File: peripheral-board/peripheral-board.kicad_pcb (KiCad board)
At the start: 2 copper layers, 165 x 100 mm, 0 parts

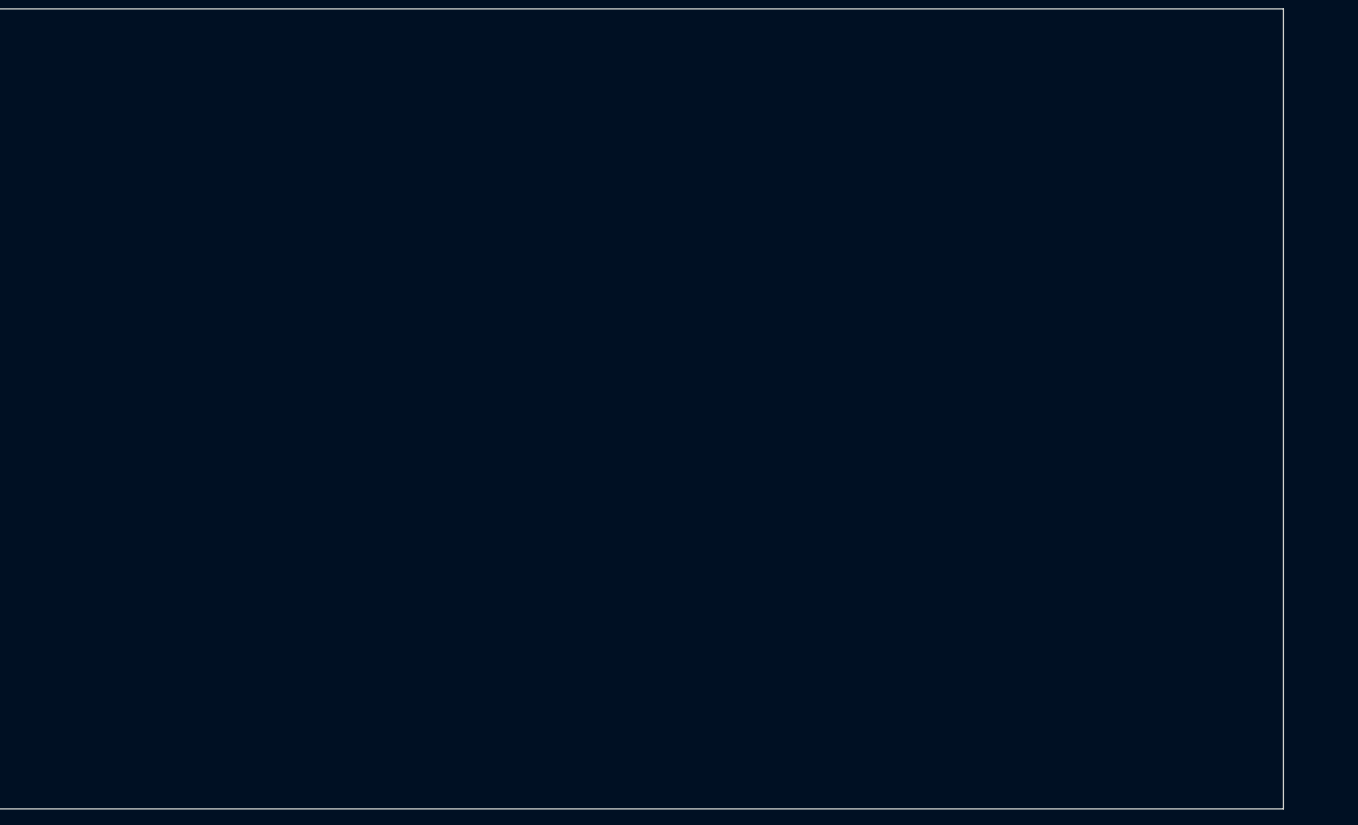
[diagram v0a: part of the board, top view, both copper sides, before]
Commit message: added button 3d model
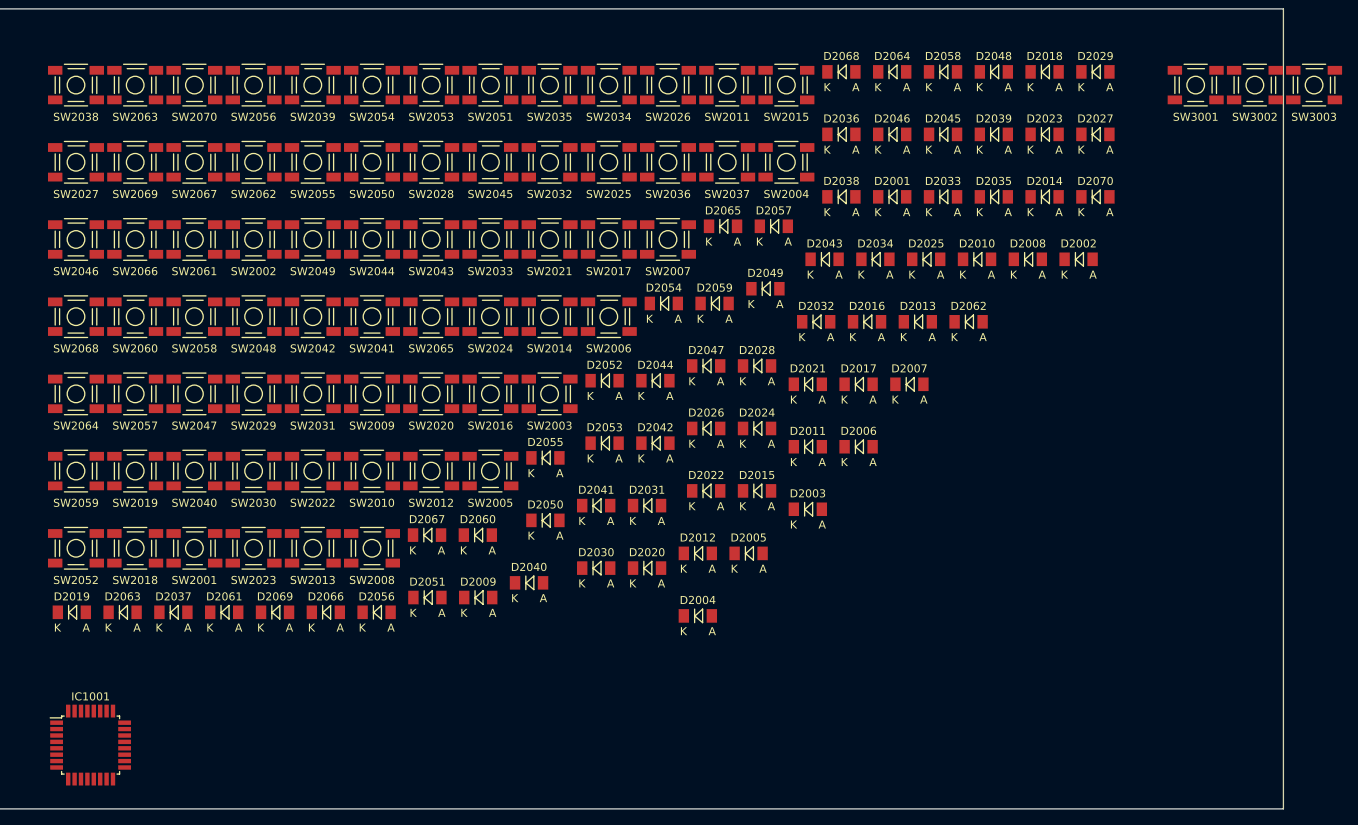
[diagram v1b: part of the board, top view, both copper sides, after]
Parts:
- added D2001: 1N4148, Diodes_SMD:MiniMELF_Standard, F.Cu at (176.1, 68.5)
- added D2002: 1N4148, Diodes_SMD:MiniMELF_Standard, F.Cu at (199.4, 76.3)
- added D2003: 1N4148, Diodes_SMD:MiniMELF_Standard, F.Cu at (165.6, 107.5)
- added D2004: 1N4148, Diodes_SMD:MiniMELF_Standard, F.Cu at (151.8, 120.9)
- added D2005: 1N4148, Diodes_SMD:MiniMELF_Standard, F.Cu at (158.2, 113.1)
- added D2006: 1N4148, Diodes_SMD:MiniMELF_Standard, F.Cu at (171.9, 99.7)
- added D2007: 1N4148, Diodes_SMD:MiniMELF_Standard, F.Cu at (178.3, 91.9)
- added D2008: 1N4148, Diodes_SMD:MiniMELF_Standard, F.Cu at (193.1, 76.3)
- added D2009: 1N4148, Diodes_SMD:MiniMELF_Standard, F.Cu at (124.4, 118.6)
- added D2010: 1N4148, Diodes_SMD:MiniMELF_Standard, F.Cu at (186.7, 76.3)
- added D2011: 1N4148, Diodes_SMD:MiniMELF_Standard, F.Cu at (165.6, 99.7)
- added D2012: 1N4148, Diodes_SMD:MiniMELF_Standard, F.Cu at (151.8, 113.1)
- added D2013: 1N4148, Diodes_SMD:MiniMELF_Standard, F.Cu at (179.3, 84.1)
- added D2014: 1N4148, Diodes_SMD:MiniMELF_Standard, F.Cu at (195.2, 68.5)
- added D2015: 1N4148, Diodes_SMD:MiniMELF_Standard, F.Cu at (159.2, 105.3)
- added D2016: 1N4148, Diodes_SMD:MiniMELF_Standard, F.Cu at (173.0, 84.1)
- added D2017: 1N4148, Diodes_SMD:MiniMELF_Standard, F.Cu at (171.9, 91.9)
- added D2018: 1N4148, Diodes_SMD:MiniMELF_Standard, F.Cu at (195.2, 52.9)
- added D2019: 1N4148, Diodes_SMD:MiniMELF_Standard, F.Cu at (73.6, 120.4)
- added D2020: 1N4148, Diodes_SMD:MiniMELF_Standard, F.Cu at (145.5, 114.9)
- added D2021: 1N4148, Diodes_SMD:MiniMELF_Standard, F.Cu at (165.6, 91.9)
- added D2022: 1N4148, Diodes_SMD:MiniMELF_Standard, F.Cu at (152.9, 105.3)
- added D2023: 1N4148, Diodes_SMD:MiniMELF_Standard, F.Cu at (195.2, 60.7)
- added D2024: 1N4148, Diodes_SMD:MiniMELF_Standard, F.Cu at (159.2, 97.4)
- added D2025: 1N4148, Diodes_SMD:MiniMELF_Standard, F.Cu at (180.4, 76.3)
- added D2026: 1N4148, Diodes_SMD:MiniMELF_Standard, F.Cu at (152.9, 97.4)
- added D2027: 1N4148, Diodes_SMD:MiniMELF_Standard, F.Cu at (201.5, 60.7)
- added D2028: 1N4148, Diodes_SMD:MiniMELF_Standard, F.Cu at (159.2, 89.6)
- added D2029: 1N4148, Diodes_SMD:MiniMELF_Standard, F.Cu at (201.5, 52.9)
- added D2030: 1N4148, Diodes_SMD:MiniMELF_Standard, F.Cu at (139.1, 114.9)
- added D2031: 1N4148, Diodes_SMD:MiniMELF_Standard, F.Cu at (145.5, 107.1)
- added D2032: 1N4148, Diodes_SMD:MiniMELF_Standard, F.Cu at (166.6, 84.1)
- added D2033: 1N4148, Diodes_SMD:MiniMELF_Standard, F.Cu at (182.5, 68.5)
- added D2034: 1N4148, Diodes_SMD:MiniMELF_Standard, F.Cu at (174.0, 76.3)
- added D2035: 1N4148, Diodes_SMD:MiniMELF_Standard, F.Cu at (188.8, 68.5)
- added D2036: 1N4148, Diodes_SMD:MiniMELF_Standard, F.Cu at (169.8, 60.7)
- added D2037: 1N4148, Diodes_SMD:MiniMELF_Standard, F.Cu at (86.3, 120.4)
- added D2038: 1N4148, Diodes_SMD:MiniMELF_Standard, F.Cu at (169.8, 68.5)
- added D2039: 1N4148, Diodes_SMD:MiniMELF_Standard, F.Cu at (188.8, 60.7)
- added D2040: 1N4148, Diodes_SMD:MiniMELF_Standard, F.Cu at (130.7, 116.7)
- added D2041: 1N4148, Diodes_SMD:MiniMELF_Standard, F.Cu at (139.1, 107.1)
- added D2042: 1N4148, Diodes_SMD:MiniMELF_Standard, F.Cu at (146.5, 99.3)
- added D2043: 1N4148, Diodes_SMD:MiniMELF_Standard, F.Cu at (167.7, 76.3)
- added D2044: 1N4148, Diodes_SMD:MiniMELF_Standard, F.Cu at (146.5, 91.5)
- added D2045: 1N4148, Diodes_SMD:MiniMELF_Standard, F.Cu at (182.5, 60.7)
- added D2046: 1N4148, Diodes_SMD:MiniMELF_Standard, F.Cu at (176.1, 60.7)
- added D2047: 1N4148, Diodes_SMD:MiniMELF_Standard, F.Cu at (152.9, 89.6)
- added D2048: 1N4148, Diodes_SMD:MiniMELF_Standard, F.Cu at (188.8, 52.9)
- added D2049: 1N4148, Diodes_SMD:MiniMELF_Standard, F.Cu at (160.3, 80.0)
- added D2050: 1N4148, Diodes_SMD:MiniMELF_Standard, F.Cu at (132.8, 108.9)
- added D2051: 1N4148, Diodes_SMD:MiniMELF_Standard, F.Cu at (118.0, 118.6)
- added D2052: 1N4148, Diodes_SMD:MiniMELF_Standard, F.Cu at (140.2, 91.5)
- added D2053: 1N4148, Diodes_SMD:MiniMELF_Standard, F.Cu at (140.2, 99.3)
- added D2054: 1N4148, Diodes_SMD:MiniMELF_Standard, F.Cu at (147.6, 81.8)
- added D2055: 1N4148, Diodes_SMD:MiniMELF_Standard, F.Cu at (132.8, 101.1)
- added D2056: 1N4148, Diodes_SMD:MiniMELF_Standard, F.Cu at (111.7, 120.4)
- added D2057: 1N4148, Diodes_SMD:MiniMELF_Standard, F.Cu at (161.3, 72.2)
- added D2058: 1N4148, Diodes_SMD:MiniMELF_Standard, F.Cu at (182.5, 52.9)
- added D2059: 1N4148, Diodes_SMD:MiniMELF_Standard, F.Cu at (153.9, 81.8)
- added D2060: 1N4148, Diodes_SMD:MiniMELF_Standard, F.Cu at (124.3, 110.8)
- added D2061: 1N4148, Diodes_SMD:MiniMELF_Standard, F.Cu at (92.6, 120.4)
- added D2062: 1N4148, Diodes_SMD:MiniMELF_Standard, F.Cu at (185.7, 84.1)
- added D2063: 1N4148, Diodes_SMD:MiniMELF_Standard, F.Cu at (79.9, 120.4)
- added D2064: 1N4148, Diodes_SMD:MiniMELF_Standard, F.Cu at (176.1, 52.9)
- added D2065: 1N4148, Diodes_SMD:MiniMELF_Standard, F.Cu at (155.0, 72.2)
- added D2066: 1N4148, Diodes_SMD:MiniMELF_Standard, F.Cu at (105.3, 120.4)
- added D2067: 1N4148, Diodes_SMD:MiniMELF_Standard, F.Cu at (118.0, 110.8)
- added D2068: 1N4148, Diodes_SMD:MiniMELF_Standard, F.Cu at (169.8, 52.9)
- added D2069: 1N4148, Diodes_SMD:MiniMELF_Standard, F.Cu at (99.0, 120.4)
- added D2070: 1N4148, Diodes_SMD:MiniMELF_Standard, F.Cu at (201.5, 68.5)
- added IC1001: ATTINY48-A, Housings_QFP:TQFP-32_7x7mm_Pitch0.8mm, F.Cu at (75.9, 137.0)
- added SW2001: 1, lib:SMD-TACT-5.2x5.2x2mm, F.Cu at (88.9, 112.4)
- added SW2002: 2, lib:SMD-TACT-5.2x5.2x2mm, F.Cu at (96.3, 73.8)
- added SW2003: 3, lib:SMD-TACT-5.2x5.2x2mm, F.Cu at (133.3, 93.1)
- added SW2004: 4, lib:SMD-TACT-5.2x5.2x2mm, F.Cu at (162.9, 64.2)
- added SW2005: 5, lib:SMD-TACT-5.2x5.2x2mm, F.Cu at (125.9, 102.8)
- added SW2006: 6, lib:SMD-TACT-5.2x5.2x2mm, F.Cu at (140.7, 83.5)
- added SW2007: 7, lib:SMD-TACT-5.2x5.2x2mm, F.Cu at (148.1, 73.8)
- added SW2008: 8, lib:SMD-TACT-5.2x5.2x2mm, F.Cu at (111.1, 112.4)
- added SW2009: 9, lib:SMD-TACT-5.2x5.2x2mm, F.Cu at (111.1, 93.1)
- added SW2010: 0, lib:SMD-TACT-5.2x5.2x2mm, F.Cu at (111.1, 102.8)
- added SW2011: 1, lib:SMD-TACT-5.2x5.2x2mm, F.Cu at (155.5, 54.5)
- added SW2012: 2, lib:SMD-TACT-5.2x5.2x2mm, F.Cu at (118.5, 102.8)
- added SW2013: 3, lib:SMD-TACT-5.2x5.2x2mm, F.Cu at (103.7, 112.4)
- added SW2014: 4, lib:SMD-TACT-5.2x5.2x2mm, F.Cu at (133.3, 83.5)
- added SW2015: 5, lib:SMD-TACT-5.2x5.2x2mm, F.Cu at (162.9, 54.5)
- added SW2016: 6, lib:SMD-TACT-5.2x5.2x2mm, F.Cu at (125.9, 93.1)
- added SW2017: 7, lib:SMD-TACT-5.2x5.2x2mm, F.Cu at (140.7, 73.8)
- added SW2018: 8, lib:SMD-TACT-5.2x5.2x2mm, F.Cu at (81.5, 112.4)
- added SW2019: 9, lib:SMD-TACT-5.2x5.2x2mm, F.Cu at (81.5, 102.8)
- added SW2020: 0, lib:SMD-TACT-5.2x5.2x2mm, F.Cu at (118.5, 93.1)
- added SW2021: Q, lib:SMD-TACT-5.2x5.2x2mm, F.Cu at (133.3, 73.8)
- added SW2022: W, lib:SMD-TACT-5.2x5.2x2mm, F.Cu at (103.7, 102.8)
- added SW2023: E, lib:SMD-TACT-5.2x5.2x2mm, F.Cu at (96.3, 112.4)
- added SW2024: R, lib:SMD-TACT-5.2x5.2x2mm, F.Cu at (125.9, 83.5)
- added SW2025: T, lib:SMD-TACT-5.2x5.2x2mm, F.Cu at (140.7, 64.2)
- added SW2026: Y, lib:SMD-TACT-5.2x5.2x2mm, F.Cu at (148.1, 54.5)
- added SW2027: U, lib:SMD-TACT-5.2x5.2x2mm, F.Cu at (74.1, 64.2)
- added SW2028: I, lib:SMD-TACT-5.2x5.2x2mm, F.Cu at (118.5, 64.2)
- added SW2029: O, lib:SMD-TACT-5.2x5.2x2mm, F.Cu at (96.3, 93.1)
- added SW2030: P, lib:SMD-TACT-5.2x5.2x2mm, F.Cu at (96.3, 102.8)
- added SW2031: Q, lib:SMD-TACT-5.2x5.2x2mm, F.Cu at (103.7, 93.1)
- added SW2032: W, lib:SMD-TACT-5.2x5.2x2mm, F.Cu at (133.3, 64.2)
- added SW2033: E, lib:SMD-TACT-5.2x5.2x2mm, F.Cu at (125.9, 73.8)
- added SW2034: R, lib:SMD-TACT-5.2x5.2x2mm, F.Cu at (140.7, 54.5)
- added SW2035: T, lib:SMD-TACT-5.2x5.2x2mm, F.Cu at (133.3, 54.5)
- added SW2036: Y, lib:SMD-TACT-5.2x5.2x2mm, F.Cu at (148.1, 64.2)
- added SW2037: U, lib:SMD-TACT-5.2x5.2x2mm, F.Cu at (155.5, 64.2)
- added SW2038: I, lib:SMD-TACT-5.2x5.2x2mm, F.Cu at (74.1, 54.5)
- added SW2039: O, lib:SMD-TACT-5.2x5.2x2mm, F.Cu at (103.7, 54.5)
- added SW2040: P, lib:SMD-TACT-5.2x5.2x2mm, F.Cu at (88.9, 102.8)
- added SW2041: A, lib:SMD-TACT-5.2x5.2x2mm, F.Cu at (111.1, 83.5)
- added SW2042: S, lib:SMD-TACT-5.2x5.2x2mm, F.Cu at (103.7, 83.5)
- added SW2043: D, lib:SMD-TACT-5.2x5.2x2mm, F.Cu at (118.5, 73.8)
- added SW2044: F, lib:SMD-TACT-5.2x5.2x2mm, F.Cu at (111.1, 73.8)
- added SW2045: G, lib:SMD-TACT-5.2x5.2x2mm, F.Cu at (125.9, 64.2)
- added SW2046: H, lib:SMD-TACT-5.2x5.2x2mm, F.Cu at (74.1, 73.8)
- added SW2047: J, lib:SMD-TACT-5.2x5.2x2mm, F.Cu at (88.9, 93.1)
- added SW2048: K, lib:SMD-TACT-5.2x5.2x2mm, F.Cu at (96.3, 83.5)
- added SW2049: L, lib:SMD-TACT-5.2x5.2x2mm, F.Cu at (103.7, 73.8)
- added SW2050: Ö, lib:SMD-TACT-5.2x5.2x2mm, F.Cu at (111.1, 64.2)
- added SW2051: A, lib:SMD-TACT-5.2x5.2x2mm, F.Cu at (125.9, 54.5)
- added SW2052: S, lib:SMD-TACT-5.2x5.2x2mm, F.Cu at (74.1, 112.4)
- added SW2053: D, lib:SMD-TACT-5.2x5.2x2mm, F.Cu at (118.5, 54.5)
- added SW2054: F, lib:SMD-TACT-5.2x5.2x2mm, F.Cu at (111.1, 54.5)
- added SW2055: G, lib:SMD-TACT-5.2x5.2x2mm, F.Cu at (103.7, 64.2)
- added SW2056: H, lib:SMD-TACT-5.2x5.2x2mm, F.Cu at (96.3, 54.5)
- added SW2057: J, lib:SMD-TACT-5.2x5.2x2mm, F.Cu at (81.5, 93.1)
- added SW2058: K, lib:SMD-TACT-5.2x5.2x2mm, F.Cu at (88.9, 83.5)
- added SW2059: L, lib:SMD-TACT-5.2x5.2x2mm, F.Cu at (74.1, 102.8)
- added SW2060: Ö, lib:SMD-TACT-5.2x5.2x2mm, F.Cu at (81.5, 83.5)
- added SW2061: Z, lib:SMD-TACT-5.2x5.2x2mm, F.Cu at (88.9, 73.8)
- added SW2062: X, lib:SMD-TACT-5.2x5.2x2mm, F.Cu at (96.3, 64.2)
- added SW2063: C, lib:SMD-TACT-5.2x5.2x2mm, F.Cu at (81.5, 54.5)
- added SW2064: V, lib:SMD-TACT-5.2x5.2x2mm, F.Cu at (74.1, 93.1)
- added SW2065: B, lib:SMD-TACT-5.2x5.2x2mm, F.Cu at (118.5, 83.5)
- added SW2066: N, lib:SMD-TACT-5.2x5.2x2mm, F.Cu at (81.5, 73.8)
- added SW2067: M, lib:SMD-TACT-5.2x5.2x2mm, F.Cu at (88.9, 64.2)
- added SW2068: ,, lib:SMD-TACT-5.2x5.2x2mm, F.Cu at (74.1, 83.5)
- added SW2069: ., lib:SMD-TACT-5.2x5.2x2mm, F.Cu at (81.5, 64.2)
- added SW2070: -, lib:SMD-TACT-5.2x5.2x2mm, F.Cu at (88.9, 54.5)
- added SW3001: Left, lib:SMD-TACT-5.2x5.2x2mm, F.Cu at (214.0, 54.5)
- added SW3002: MIddle, lib:SMD-TACT-5.2x5.2x2mm, F.Cu at (221.4, 54.5)
- added SW3003: Right, lib:SMD-TACT-5.2x5.2x2mm, F.Cu at (228.8, 54.5)
